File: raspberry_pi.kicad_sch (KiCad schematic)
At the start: 11 parts, among them J2 Raspberry_Pi, U4 ATECC608A-MAHDA

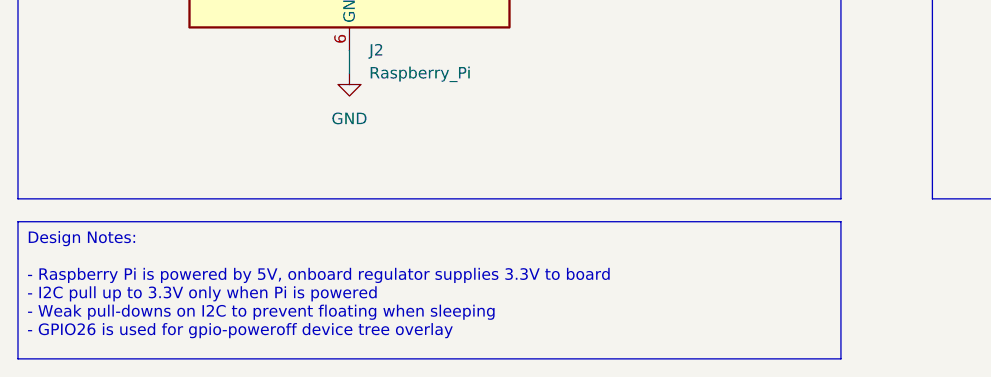
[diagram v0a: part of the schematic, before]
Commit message: update to kicad 9.0
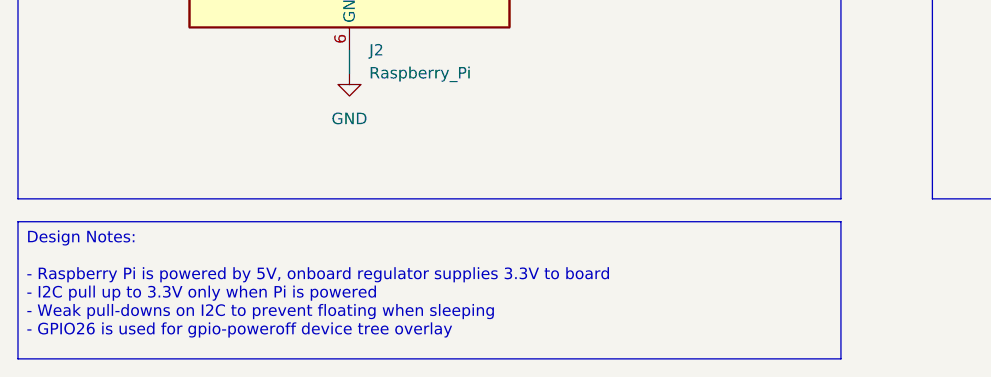
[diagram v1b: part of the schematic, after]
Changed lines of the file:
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@@
 (kicad_sch
-	(version 20231120)
+	(version 20250114)
 	(generator "eeschema")
-	(generator_version "8.0")
+	(generator_version "9.0")
 	(paper "A4")
 	(title_block
@@
 		(comment 4 "Raspberry Pi, NervesKey and mechanical spec")
 	)
+	(rectangle
+		(start 163.83 35.56)
+		(end 229.87 76.2)
+		(stroke
+			(width 0)
+			(type default)
+		)
+		(fill
+			(type none)
+		)
+	)
+	(rectangle
+		(start 62.23 35.56)
+		(end 153.67 134.62)
+		(stroke
+			(width 0)
+			(type default)
+		)
+		(fill
+			(type none)
+		)
+	)
+	(rectangle
+		(start 163.83 85.09)
+		(end 229.87 134.62)
+		(stroke
+			(width 0)
+			(type default)
+		)
+		(fill
+			(type none)
+		)
+	)
+	(text "NervesKey"
+		(exclude_from_sim no)
+		(at 163.83 33.02 0)
+		(effects
+			(font
+				(size 2 2)
+				(thickness 0.4)
+				(bold yes)
+			)
+			(justify left)
+		)
+	)
+	(text "Mounting Holes"
+		(exclude_from_sim no)
+		(at 163.83 82.55 0)
+		(effects
+			(font
+				(size 2 2)
+				(thickness 0.4)
+				(bold yes)
+			)
+			(justify left)
+		)
+	)
+	(text "Raspberry Pi"
+		(exclude_from_sim no)
+		(at 66.04 33.02 0)
+		(effects
+			(font
+				(size 2 2)
+				(thickness 0.4)
+				(bold yes)
+			)
+			(justify left)
+		)
+	)
+	(text_box "Design Notes:\n\n- Raspberry Pi is powered by 5V, onboard regulator supplies 3.3V to board\n- I2C pull up to 3.3V only when Pi is powered\n- Weak pull-downs on I2C to prevent floating when sleeping\n- GPIO26 is used for gpio-poweroff device tree overlay"
+		(exclude_from_sim no)
+		(at 62.23 137.16 0)
+		(size 91.44 15.24)
+		(margins 0.9525 0.9525 0.9525 0.9525)
+		(stroke
+			(width 0)
+			(type default)
+		)
+		(fill
+			(type color)
+			(color 255 255 194 1)
+		)
+		(effects
+			(font
+				(size 1.27 1.27)
+			)
+			(justify left top)
+		)
+	)
 	(junction
 		(at 134.62 72.39)
@@
 			(width 0)
 			(type default)
-		)
-	)
-	(rectangle
-		(start 163.83 35.56)
-		(end 229.87 76.2)
-		(stroke
-			(width 0)
-			(type default)
-		)
-		(fill
-			(type none)
-		)
-	)
-	(rectangle
-		(start 62.23 35.56)
-		(end 153.67 134.62)
-		(stroke
-			(width 0)
-			(type default)
-		)
-		(fill
-			(type none)
-		)
-	)
-	(rectangle
-		(start 163.83 85.09)
-		(end 229.87 134.62)
-		(stroke
-			(width 0)
-			(type default)
-		)
-		(fill
-			(type none)
 		)
 	)
@@
 			"AAEIQAACEIAABCDgKwI4R3x1ueksBCAAAQhAAAIQgAAEIAABCEAAAsEEcI4EE+E9BCAAAQhAAAIQ"
 			"gAAEIAABCEAAAr4igHPEV5ebzkIAAhCAAAQgAAEIQAACEIAABCAQTOD/Aai05xHM4wJQAAAAAElF"
-			"TkSuQmCC"
-		)
-	)
-	(text_box "Design Notes:\n\n- Raspberry Pi is powered by 5V, onboard regulator supplies 3.3V to board\n- I2C pull up to 3.3V only when Pi is powered\n- Weak pull-downs on I2C to prevent floating when sleeping\n- GPIO26 is used for gpio-poweroff device tree overlay"
-		(exclude_from_sim no)
-		(at 62.23 137.16 0)
-		(size 91.44 15.24)
-		(stroke
-			(width 0)
-			(type default)
-		)
-		(fill
-			(type color)
-			(color 255 255 194 1)
-		)
-		(effects
-			(font
-				(size 1.27 1.27)
-			)
-			(justify left top)
-		)
-	)
-	(text "NervesKey"
-		(exclude_from_sim no)
-		(at 163.83 33.02 0)
-		(effects
-			(font
-				(size 2 2)
-				(thickness 0.4)
-				(bold yes)
-			)
-			(justify left)
-		)
-	)
-	(text "Mounting Holes"
-		(exclude_from_sim no)
-		(at 163.83 82.55 0)
-		(effects
-			(font
-				(size 2 2)
-				(thickness 0.4)
-				(bold yes)
-			)
-			(justify left)
-		)
-	)
-	(text "Raspberry Pi"
-		(exclude_from_sim no)
-		(at 66.04 33.02 0)
-		(effects
-			(font
-				(size 2 2)
-				(thickness 0.4)
-				(bold yes)
-			)
-			(justify left)
+			"TkSuQmCCAAAAAAAAAAAAAAAAAAAAAAAAAAAAAAAAAAAAAAAAAAAAAAAAAAAAAAAAAAAAAAAAAAAA"
+			"AAAAAAAAAAAAAAAAAAAAAAAAAAAAAAAAAAAAAAAAAAAAAAAAAAAAAAAAAAAAAAAAAAAAAAAAAAAA"
+			"AAAAAAAAAAAAAAAAAAAAAAAAAAAAAAAAAAAAAAAAAAAAAAAAAAAAAAAAAAAAAAAAAAAAAAAAAAAA"
+			"AAAAAAAAAAAAAAAAAAAAAAAAAAAAAAAAAAAAAAAAAAAAAAAAAAAAAAAAAAAAAAAAAAAAAAAAAAAA"
+			"AAAAAAAAAAAAAAAAAAAAAAAAAAAAAAAAAAAAAAAAAAAAAAAAAAAAAAAAAAAAAAAAAAAAAAAAAAAA"
+			"AAAAAAAAAAAAAAAAAAAAAAAAAAAAAAAAAAAAAAAAAAAAAAAAAAAAAAAAAAAAAAAAAAAAAAAAAAAA"
+			"AAAAAAAAAAAAAAAAAAAAAAAAAAAAAAAAAAAAAAAAAAAAAAAAAAAAAAAAAAAAAAAAAAAAAAAAAAAA"
+			"AAAAAAAAAAAAAAAAAAAAAAAAAAAAAAAAAAAAAAAAAAAAAAAAAAAAAAAAAAAAAAAAAAAAAAAAAAAA"
+			"AAAAAAAAAAAAAAAAAAAAAAAAAAAAAAAAAAAAAAAAAAAAAAAAAAAAAAAAAAAAAAAAAAAAAAAAAAAA"
+			"AAAAAAAAAAAAAAAAAAAAAAAAAAAAAAAAAAAAAAAAAAAAAAAAAAAAAAAAAAAAAAAAAAAAAAAAAAAA"
+			"AAAAAAAAAAAAAAAAAAAAAAAAAAAAAAAAAAAAAAAAAAAAAAAAAAAAAAAAAAAAAAAAAAAAAAAAAAAA"
+			"AAAAAAAAAAAAAAAAAAAAAAAAAAAAAAAAAAAAAAAAAAAAAAAAAAAAAAAAAAAAAAAAAAAAAAAAAAAA"
+			"AAAAAAAAAAAAAAAAAAAAAAAAAAAAAAAAAAAAAAAAAAAAAAAAAAAAAAAAAAAAAAAAAAAAAAAAAAAA"
+			"AAAAAAAAAAAAAAAAAAAAAAAAAAAAAAAAAAAAAAAAAAAAAAAAAAAAAAAAAAAAAAAAAAAAAAAAAAAA"
+			"AAAAAAAAAAAAAAAAAAAAAAAAAAAAAAAAAAAAAAAAAAAAAAAAAAAAAAAAAAAAAAAAAAAAAAAAAAAA"
+			"AAAAAAAAAAAAAAAAAAAAAAAAAAAAAAAAAAAAAAAAAAAAAAAAAAAAAAAAAAAAAAAAAAAAAAAAAAAA"
+			"AAAAAAAAAAAAAAAAAAAAAAAAAAAAAAAAAAAAAAAAAAAAAAAAAAAAAAAAAAAAAAAAAAAAAAAAAAAA"
+			"AAAAAAAAAAAAAAAAAAAAAAAAAAAAAAAAAAAAAAAAAAAAAAAAAAAAAAAAAAAAAAAAAAAAAAAAAAAA"
+			"AAAAAAECBAj8BQTe/8cWEiBAgAABAgQIECBAgAABAgQIECBAgAABAgQIECAwERB4J0eaQYAAAQIE"
+			"CBAgQIAAAQIECBAgQIAAAQIECBAgQIDAX0Dg/X9sIQECBAgQIECAAAECBAgQIECAAAECBAgQIECA"
+			"AAECEwGBd3KkGQQIECBAAAAseAAAAABo2syF2H8AAAIAAAABAgQI0N0cFtl/AAAAAAAAAAAAAAAA"
+			"AAAAAAAAAAAAAAAAAAAAAAAAMBEITgCAy4XYfwAAAAAAAAEAAACAYIIUAQAAACAHDJzYfwAA4NjM"
+			"hdh/AAAg6lMlAQAAAHCPUSUBAAAAMONqFAEAAABwj1ElAQAAAFDqUyUBAAAAsPhVJQEAAACQ42oU"
+			"AQAAALD4VSUBAAAA4OpqFAEAAABwj1ElAQAAAIDqUyUBAAAA8ItRJQEAAAAw42oUAQAAAPCLUSUB"
+			"AAAAsOpTJQEAAACwM2IUAQAAABBuahQBAAAA4OpTJQEAAACw91UlAQAAAJDjahQBAAAAsDNiFAEA"
+			"AADg6moUAQAAAPCLUSUBAAAAEOtTJQEAAACwM2IUAQAAABBuahQBAAAAsDNiFAEAAABA61MlAQAA"
+			"ADD4VSUBAAAA4OpqFAEAAACwM2IUAQAAAHDrUyUBAAAAsDNiFAEAAAAQbmoUAQAAALAzYhQBAAAA"
+			"oOtTJQEAAADw9lUlAQAAAEDrahQBAAAAsDNiFAEAAABQHWMUAQAAAHCPUSUBAAAA8ItRJQEAAACw"
+			"M2IUAQAAALAzYhQBAAAAUB1jFAEAAADQ61MlAQAAAADsUyUBAAAA8BxoFAEAAACA6moUAQAAADDs"
+			"UyUBAAAAsDNiFAEAAADg6moUAQAAAGDsUyUBAAAAsMlRJQEAAABA62oUAQAAALDJUSUBAAAAsDNi"
+			"FAEAAACwyVElAQAAALDJUSUBAAAAsDNiFAEAAACwyVElAQAAALDJUSUBAAAAsDNiFAEAAACwyVEl"
+			"AQAAAAAALXgAAAAAYNnMhdh/AAADAAAAAQAAAODlHBbZfwAAAAAAAAAAAAAAAAAAAAAAAAAAAAAA"
+			"AAAAAAAAAAEAAAAAgMuF2H8AAAAAACAAAAAAwOxTJQEAAAAgBwyc2H8AANjXzIXYfwAAAAAAEAEA"
+			"DgAAAAAAkuAHALAzYhQBAAAA4OpqFAEAAACwM2IUAQAAALAzYhQBAAAAsDNiFAEAAAAg7VMlAQAA"
+			"ALDJUSUBAAAA4OpqFAEAAACwyVElAQAAALDJUSUBAAAAUO1TJQEAAACwM2IUAQAAABBuahQBAAAA"
+			"sDNiFAEAAACA7VMlAQAAADAQVSUBAAAAgOpqFAEAAABA62oUAQAAAEDrahQBAAAAsDNiFAEAAABQ"
+			"HWMUAQ=="
 		)
 	)
@@
 		(shape input)
 		(at 93.98 49.53 90)
-		(fields_autoplaced yes)
 		(effects
 			(font
@@
 		(shape bidirectional)
 		(at 209.55 53.34 0)
-		(fields_autoplaced yes)
 		(effects
 			(font
@@
 		(shape output)
 		(at 181.61 50.8 90)
-		(fields_autoplaced yes)
 		(effects
 			(font
@@
 		(shape bidirectional)
 		(at 138.43 69.85 0)
-		(fields_autoplaced yes)
 		(effects
 			(font
@@
 		(shape bidirectional)
 		(at 138.43 72.39 0)
-		(fields_autoplaced yes)
 		(effects
 			(font
@@
 		(shape bidirectional)
 		(at 209.55 58.42 0)
-		(fields_autoplaced yes)
 		(effects
 			(font
@@
 		(shape output)
 		(at 198.12 46.99 90)
-		(fields_autoplaced yes)
 		(effects
 			(font
@@
 		(shape output)
 		(at 132.08 58.42 90)
-		(fields_autoplaced yes)
 		(effects
 			(font
@@
 		(shape output)
 		(at 73.66 100.33 180)
-		(fields_autoplaced yes)
 		(effects
 			(font
@@
 		(shape output)
 		(at 104.14 49.53 90)
-		(fields_autoplaced yes)
 		(effects
 			(font
